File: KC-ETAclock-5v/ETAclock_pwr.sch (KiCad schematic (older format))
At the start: 26 parts, among them J5 USB_SUPPLY

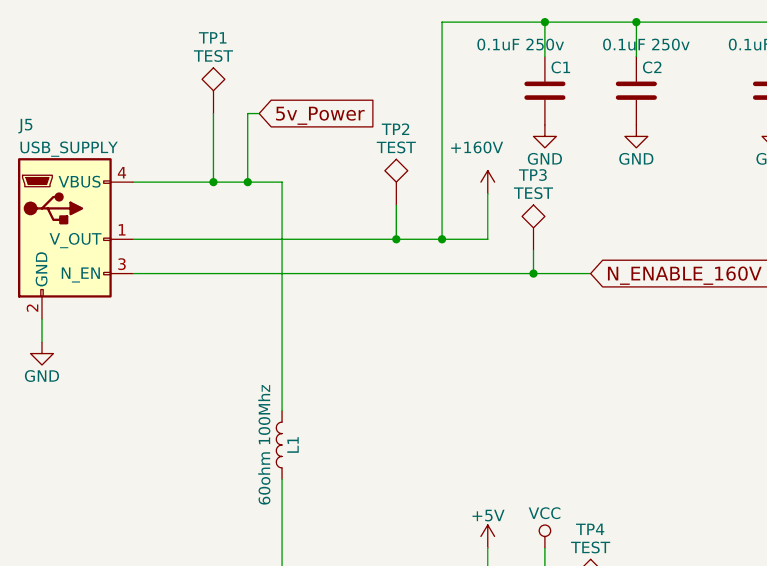
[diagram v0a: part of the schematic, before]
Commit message: New Layout changes.  Fixed the BJT packages.  Added 1k to the 160v_enable pin to protect the rasberry pi.  Improved the 160v spacing to the power supply input.
updated the code with both a testscript and a testETAclock.py to help test the code.
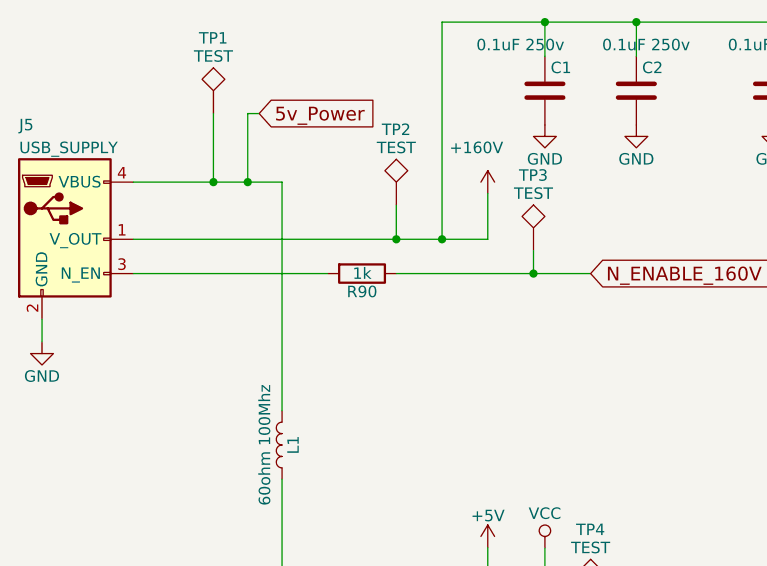
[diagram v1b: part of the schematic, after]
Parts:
- added R90: 1k, Resistors_SMD:R_0805, symbol R
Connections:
- net N_ENABLE_160V: now also R90.1; no longer J5.3 (N_EN)
- new net: J5.3 (N_EN), R90.2
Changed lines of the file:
@@
 	4600 2100 4600 1800
-Wire Wire Line
-	4250 2500 6250 2500
 Wire Wire Line
 	4900 2100 4900 3100
@@
 Wire Wire Line
 	4750 1800 4750 2100
+$Comp
+L R R90
+U 1 1 5AAB76D1
+P 5250 2500
+F 0 "R90" V 5330 2500 50  0000 C CNN
+F 1 "1k" V 5250 2500 50  0000 C CNN
+F 2 "Resistors_SMD:R_0805" V 5180 2500 50  0001 C CNN
+F 3 "" H 5250 2500 50  0001 C CNN
+	1    5250 2500
+	0    1    1    0
+$EndComp
+Wire Wire Line
+	5400 2500 6250 2500
+Wire Wire Line
+	5100 2500 4250 2500
 $EndSCHEMATC
